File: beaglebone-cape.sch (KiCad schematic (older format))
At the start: 9 parts, among them J1 CONN_2X2, P1 BEAGLEBONE_BLACK, U1 24C16

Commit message: Create the io cape base on the barebone cape
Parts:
- removed J1: CONN_2X2, symbol CONN_2X2
- added C10, C11, C3, C4, C5, C6, C8, C9: C, Capacitors_SMD:C_0805, symbol C
- added C2, C7: CP2, Capacitors_SMD:c_elec_6.3x5.7, symbol CP2
- added CON1: USB-MICRO-B, Connect:USB_Micro-B, symbol USB-MICRO-B
- added J1: CONN_02X02, Pin_Headers:Pin_Header_Straight_2x02, symbol CONN_02X02
- added J5vSelect1: CONN_01X03, Pin_Headers:Pin_Header_Straight_1x03, symbol CONN_01X03
- added J_ADC_REF1, P_PWR1: CONN_01X02, Pin_Headers:Pin_Header_Straight_1x02, symbol CONN_01X02
- added P0+1, P0-1, P0S1, P1+1, P1-1, P1S1, P2+1, P2-1, P2S1, P8, PIO1, PIO_3V3, PIO_5V1, PIO_GND1, P_AD+1, P_AD-1, P_AD1: CONN_01X08, Pin_Headers:Pin_Header_Straight_1x08, symbol CONN_01X08
- added UADC1: ADS7828, Housings_SSOP:TSSOP-16_4.4x5mm_Pitch0.65mm, symbol ADS7828
- added UP0, UP1, UP2, UPIO1: TXS0108E, Housings_SSOP:TSSOP-20_4.4x6.5mm_Pitch0.65mm, symbol TXS0108E
- added U_IMU1: BMX055-Breakout, Pin_Headers:Pin_Header_Straight_1x10, symbol BMX055-Breakout
- C1: footprint ~ -> Capacitors_SMD:C_0805
- P1: footprint ~ -> BeagleBoneBlack Cape:BEAGLEBONE_BLACK
- R1, R2, R3, R4, R5: footprint ~ -> Resistors_SMD:R_0805
- U_EEPROM1: renamed from U1; footprint (none) -> SMD_Packages:SOIC-8-W
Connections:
- net labels added: ECAPPWM0, ECAPPWM2, EHRPWM0A, EHRPWM0B, P_GPIO_32, P_GPIO_33, P_GPIO_34, P_GPIO_35, P_GPIO_36, P_GPIO_37, P_GPIO_38, P_GPIO_39, P_GPIO_70, P_GPIO_71, P_GPIO_72, P_GPIO_73, P_GPIO_74, P_GPIO_75, P_GPIO_76, P_GPIO_77, P_I2C2_SCL, P_I2C2_SDA, P_PWM_P8_13, P_PWM_P8_19, P_PWM_P9_14, P_PWM_P9_16, P_PWM_P9_28, P_PWM_P9_29, P_PWM_P9_31, P_PWM_P9_42, P_SPI0_CS0, P_SPI0_D0, P_SPI0_D1, P_SPI0_SCLK, P_UART1_RXD, P_UART1_TXD, SHLD_5V, SPI0_CS0, SPI0_D0, SPI0_D1, SPI0_SCLK
- wire segments 24 -> 117
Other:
- note removed: "BEAGLEBONE HEADERS"
- moved on the sheet: C1, P1A, P1B, R1, R2, R3, R4, R5, U_EEPROM1

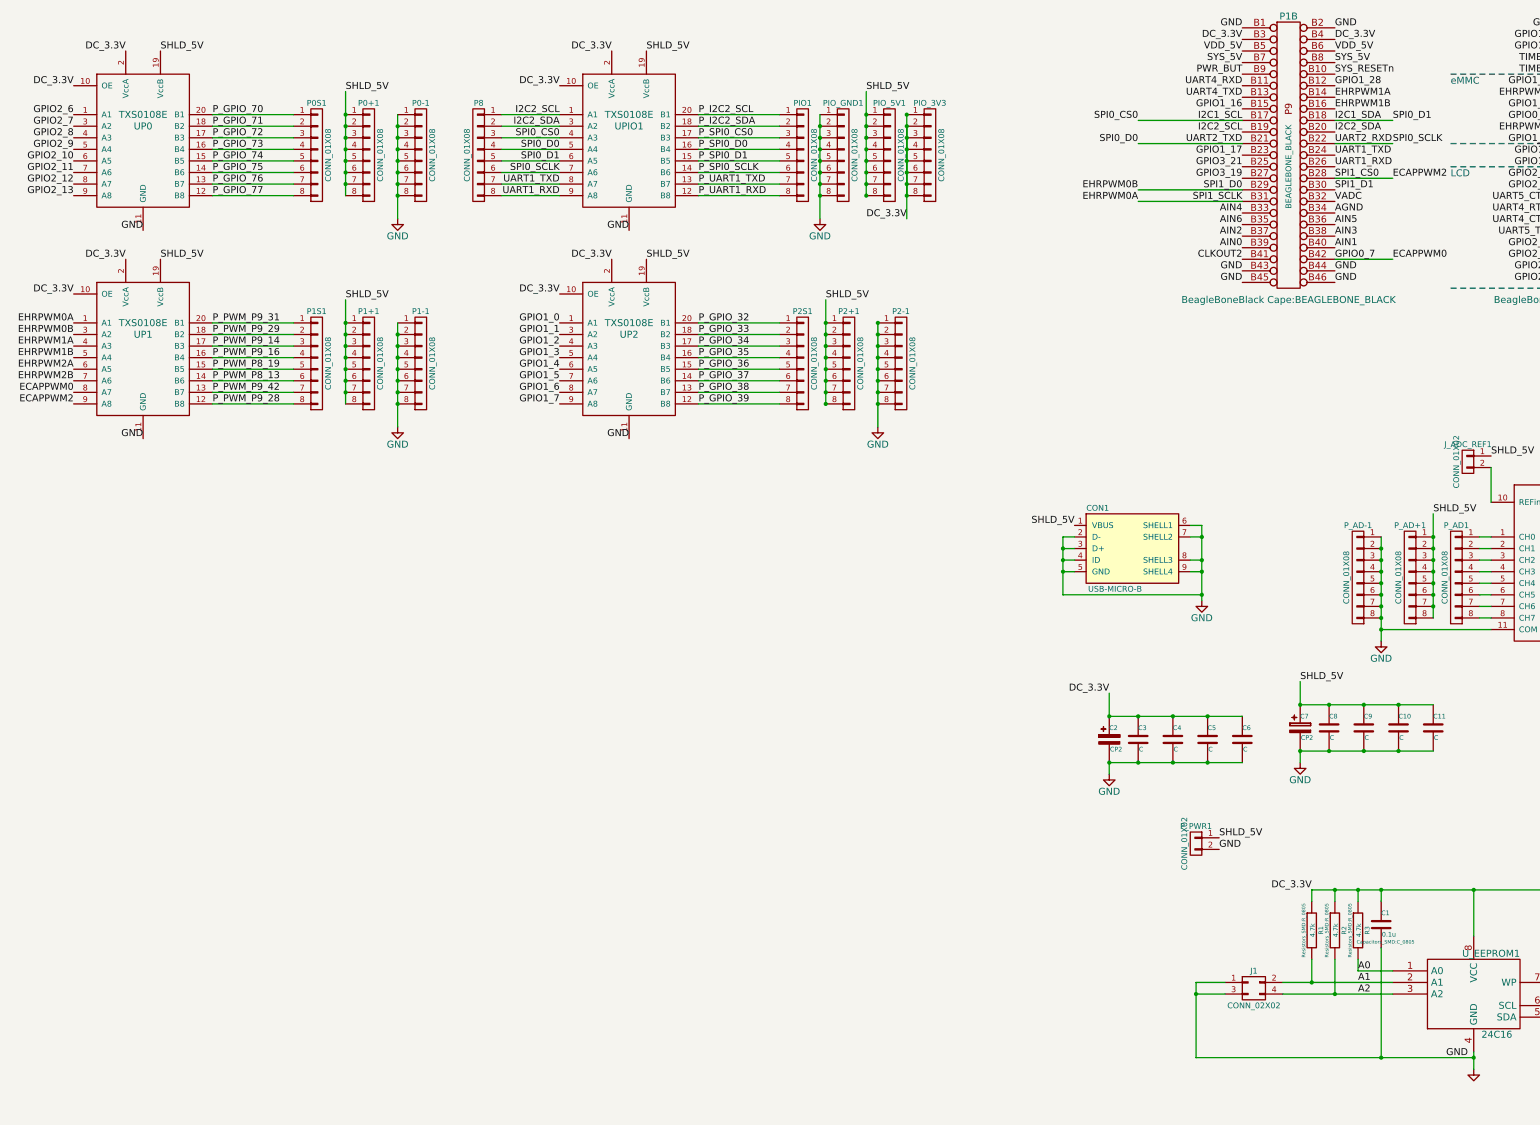
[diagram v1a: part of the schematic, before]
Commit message: Added new symbols for new ICs, created gitignore
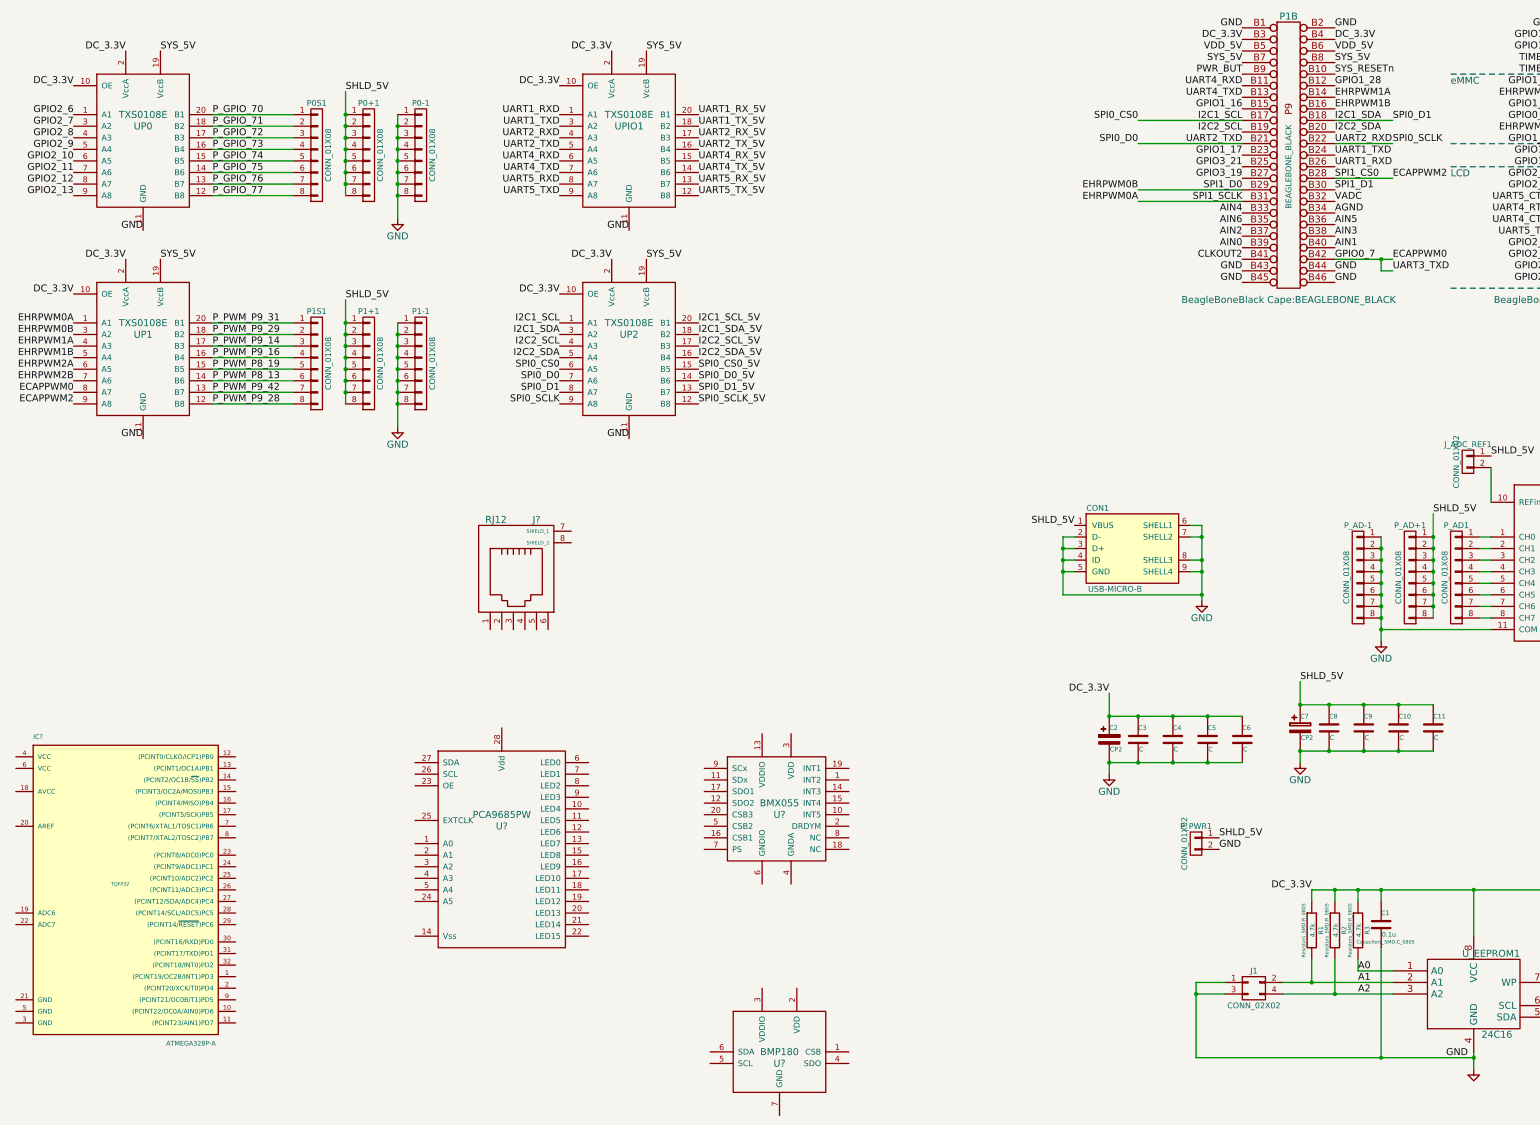
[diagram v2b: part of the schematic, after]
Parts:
- removed P2+1, P2-1, P2S1, P8, PIO1, PIO_3V3, PIO_5V1, PIO_GND1: CONN_01X08, Pin_Headers:Pin_Header_Straight_1x08, symbol CONN_01X08
- added IC?: ATMEGA328P-A, TQFP32, symbol ATMEGA328P-A
- added J?: RJ12, symbol RJ12
- added U?: PCA9685PW, symbol PCA9685PW
- added U?: BMX055, symbol BMX055
- added U?: BMP180, symbol BMP180
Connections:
- net GPIO1_0: no longer UP2.1 (A1)
- net GPIO1_1: no longer UP2.3 (A2)
- net GPIO1_2: no longer UP2.4 (A3)
- net GPIO1_3: no longer UP2.5 (A4)
- net GPIO1_4: no longer UP2.6 (A5)
- net GPIO1_5: no longer UP2.7 (A6)
- net GPIO1_6: no longer UP2.8 (A7)
- net GPIO1_7: no longer UP2.9 (A8)
- net I2C1_SCL: now also UP2.1 (A1), UP2.6 (A5); no longer UPIO1.4 (A3)
- net I2C1_SDA: now also UP2.3 (A2), UP2.8 (A7); no longer UPIO1.6 (A5)
- net I2C2_SCL: now also UP2.4 (A3); no longer UPIO1.1 (A1)
- net I2C2_SDA: now also UP2.5 (A4); no longer UPIO1.3 (A2)
- net P_I2C2_SCL: no longer UPIO1.20 (B1)
- net P_I2C2_SDA: no longer UPIO1.18 (B2)
- net SHLD_5V: no longer UP0.19 (VccB), UP1.19 (VccB), UP2.19 (VccB), UPIO1.19 (VccB)
- net SPI0_D0: now also UP2.7 (A6)
- net SPI0_SCLK: now also UP2.9 (A8), UPIO1.4 (A3); no longer UPIO1.7 (A6)
- net SYS_5V: now also UP0.19 (VccB), UP1.19 (VccB), UP2.19 (VccB), UPIO1.19 (VccB)
- net UART1_RXD: now also UPIO1.1 (A1); no longer UPIO1.9 (A8)
- net UART1_TXD: now also UPIO1.3 (A2); no longer UPIO1.8 (A7)
- net UART4_RXD: now also UPIO1.6 (A5)
- net UART4_TXD: now also UPIO1.7 (A6)
- net UART5_RXD: now also UPIO1.8 (A7)
- net UART5_TXD: now also UPIO1.9 (A8)
- net P_GPIO_32 renamed I2C1_SCL_5V
- net P_GPIO_33 renamed I2C1_SDA_5V
- net P_GPIO_34 renamed I2C2_SCL_5V
- net P_GPIO_35 renamed I2C2_SDA_5V
- net P_GPIO_36 renamed SPI0_CS0_5V
- net P_GPIO_37 renamed SPI0_D0_5V
- net P_GPIO_38 renamed SPI0_D1_5V
- net P_GPIO_39 renamed SPI0_SCLK_5V
- net P_SPI0_CS0 renamed UART2_RX_5V
- net P_SPI0_D0 renamed UART2_TX_5V
- net P_SPI0_D1 renamed UART4_RX_5V
- net P_SPI0_SCLK renamed UART4_TX_5V
- net P_UART1_RXD renamed UART5_TX_5V
- net P_UART1_TXD renamed UART5_RX_5V
- new net UART1_RX_5V: UPIO1.20 (B1)
- new net UART1_TX_5V: UPIO1.18 (B2)

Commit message: Create schematics for plane shield
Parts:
- removed U_IMU1: BMX055-Breakout, Pin_Headers:Pin_Header_Straight_1x10, symbol BMX055-Breakout
- added C? (x3): 0.1uf, symbol C
- added D?: LED, symbol LED
- added J? (x4): RJ12, symbol RJ12
- added JP? (x2): JUMPER, symbol JUMPER
- added P? (x3): CONN_01X14, symbol CONN_01X14
- added P?: CONN_01X02, symbol CONN_01X02
- added P?: CONN_02X08, symbol CONN_02X08
- added P?: CONN_02X03, symbol CONN_02X03
- added P? (x4): CONN_01X06, symbol CONN_01X06
- added P?: CONN_01X04, symbol CONN_01X04
- added PPM_IN1, SERIAL_IN: CONN_01X03, symbol CONN_01X03
- added R?: 330, symbol R
- added R?: 10K, symbol R
- added R?: 10k, symbol R
- added SW?: SW_PUSH, symbol SW_PUSH
- added X?: CRYSTAL_SMD, symbol CRYSTAL_SMD
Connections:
- net A0: now also IC?.23 ((PCINT8/ADC0)PC0), P?.10 (P10)
- net A1: now also IC?.24 ((PCINT9/ADC1)PC1), P?.12 (P12)
- net A2: now also IC?.25 ((PCINT10/ADC2)PC2), P?.14 (P14)
- net DC_3.3V: now also U?.13 (VDDIO), U?.2 (VDD), U?.3 (VDD), U?.3 (VDDIO), U?.7 (PS); no longer UP0.10 (OE), UP1.10 (OE), UP2.10 (OE), UPIO1.10 (OE)
- net GND: now also IC?.21 (GND), IC?.3 (GND), IC?.5 (GND), J?.2, U?.1 (A0), U?.12 (SDO2), U?.14 (Vss), U?.17 (SDO1), U?.2 (A1), U?.20 (CSB3), U?.24 (A5), U?.25 (EXTCLK), U?.3 (A2), U?.4 (A3), U?.4 (GNDA), U?.5 (A4), U?.6 (GNDIO), U?.7 (GND), C?.2, C?.2, D?.2 (K), J?.2, J?.2, J?.2, J?.2, P?.1 (P1), P?.1 (P1), P?.10 (P10), P?.11 (P11), P?.12 (P12), P?.13 (P13), P?.14 (P14), P?.2 (P2), P?.2 (P2), P?.3 (P3), P?.4 (P4), P?.4 (P4), P?.5 (P5), P?.6 (P6), P?.6 (P6), P?.6 (P6), P?.6 (P6), P?.6 (P6), P?.7 (P7), P?.8 (P8), P?.9 (P9), PPM_IN1.3 (P3), SERIAL_IN.2 (P2), SW?.2, X?.3 (case)
- net I2C2_SCL: now also U?.5 (SCL), U?.9 (SCx)
- net I2C2_SCL_5V: now also J?.1, JP?.2, P?.2 (P2)
- net I2C2_SDA: now also U?.11 (SDx), U?.6 (SDA)
- net I2C2_SDA_5V: now also J?.6, JP?.2, P?.3 (P3)
- net SHLD_5V: no longer CON1.1 (VBUS), J5vSelect1.2 (P2), J_ADC_REF1.1 (P1), P0+1.1 (P1), P0+1.2 (P2), P0+1.3 (P3), P0+1.4 (P4), P0+1.5 (P5), P0+1.6 (P6), P0+1.7 (P7), P0+1.8 (P8), P1+1.1 (P1), P1+1.2 (P2), P1+1.3 (P3), P1+1.4 (P4), P1+1.5 (P5), P1+1.6 (P6), P1+1.7 (P7), P1+1.8 (P8), P_AD+1.1 (P1), P_AD+1.2 (P2), P_AD+1.3 (P3), P_AD+1.4 (P4), P_AD+1.5 (P5), P_AD+1.6 (P6), P_AD+1.7 (P7), P_AD+1.8 (P8), UADC1.16 (Vdd)
- net SPI0_CS0_5V: now also J?.1
- net SPI0_D0_5V: now also J?.3
- net SPI0_D1_5V: now also J?.4
- net SPI0_SCLK_5V: now also J?.6
- net SYS_5V: now also J_ADC_REF1.1 (P1), UADC1.16 (Vdd)
- net SYS_RESETn: now also UP0.10 (OE), UP1.10 (OE), UP2.10 (OE), UPIO1.10 (OE)
- net UART1_RX_5V: now also J?.4, P?.3 (P3)
- net UART1_TX_5V: now also J?.3, P?.2 (P2)
- net UART2_RX_5V: now also J?.4, P?.3 (P3)
- net UART2_TX_5V: now also J?.3, P?.2 (P2)
- net UART4_RX_5V: now also J?.4, P?.3 (P3)
- net UART4_TX_5V: now also J?.3, P?.2 (P2)
- net UART5_RX_5V: now also IC?.31 ((PCINT17/TXD)PD1), J?.4, P?.5 (P5)
- net UART5_TX_5V: now also IC?.30 ((PCINT16/RXD)PD0), J?.3, P?.4 (P4), SERIAL_IN.1 (P1)
- net D3: now reaches IC?.1 ((PCINT19/OC2B/INT1)PD3)
- net D3: now also P?.3 (P3)
- net D6: now reaches IC?.10 ((PCINT22/OC0A/AIN0)PD6)
- net D6: now also P?.9 (P9)
- net D7: now reaches IC?.11 ((PCINT23/AIN1)PD7)
- net D7: now also P?.11 (P11)
- net D8: now reaches IC?.12 ((PCINT0/CLKO/ICP1)PB0)
- net D8: now also P?.13 (P13)
- net D9: now reaches IC?.13 ((PCINT1/OC1A)PB1)
- net D9: now also P?.15 (P15)
- net D10: now reaches IC?.14 ((PCINT2/OC1B/~SS~)PB2)
- net D10: now also P?.2 (P2)
- net D11: now reaches IC?.15 ((PCINT3/OC2A/MOSI)PB3)
- net D11: now also P?.4 (P4), P?.4 (P4)
- net D12: now reaches IC?.16 ((PCINT4/MISO)PB4)
- net D12: now also P?.1 (P1), P?.6 (P6)
- net D13: now reaches IC?.17 ((PCINT5/SCK)PB5)
- net D13: now also P?.3 (P3), P?.8 (P8), R?.1
- net PWR_5V: now reaches IC?.18 (AVCC)
- net PWR_5V: now also CON1.1 (VBUS), IC?.4 (VCC), IC?.6 (VCC), J5vSelect1.2 (P2), J?.5, P0+1.1 (P1), P0+1.2 (P2), P0+1.3 (P3), P0+1.4 (P4), P0+1.5 (P5), P0+1.6 (P6), P0+1.7 (P7), P0+1.8 (P8), P1+1.1 (P1), P1+1.2 (P2), P1+1.3 (P3), P1+1.4 (P4), P1+1.5 (P5), P1+1.6 (P6), P1+1.7 (P7), P1+1.8 (P8), P_AD+1.1 (P1), P_AD+1.2 (P2), P_AD+1.3 (P3), P_AD+1.4 (P4), P_AD+1.5 (P5), P_AD+1.6 (P6), P_AD+1.7 (P7), P_AD+1.8 (P8), U?.28 (Vdd), C?.1, J?.5, J?.5, J?.5, J?.5, P?.1 (P1), P?.1 (P1), P?.1 (P1), P?.1 (P1), P?.2 (P2), P?.2 (P2), P?.3 (P3), PPM_IN1.2 (P2), R?.1, R?.1, SERIAL_IN.3 (P3)
- net D4: now reaches IC?.2 ((PCINT20/XCK/T0)PD4)
- net D4: now also P?.5 (P5)
- net at IC?.20 (AREF): now also C?.1
- net A3: now reaches IC?.26 ((PCINT11/ADC3)PC3)
- net A3: now also P?.16 (P16)
- net PWM_SDA: now reaches IC?.27 ((PCINT12/SDA/ADC4)PC4)
- net PWM_SDA: now also U?.27 (SDA), JP?.1
- net PWM_SCL: now reaches IC?.28 ((PCINT14/SCL/ADC5)PC5)
- net PWM_SCL: now also U?.26 (SCL), JP?.1
- net A_RST: now reaches IC?.29 ((PCINT14/~RESET~)PC6)
- net A_RST: now also C?.2, P?.5 (P5), R?.2, SW?.1
- net D2: now reaches IC?.32 ((PCINT18/INT0)PD2)
- net D2: now also P?.1 (P1), PPM_IN1.1 (P1)
- net at IC?.7 ((PCINT6/XTAL1/TOSC1)PB6): now also X?.2
- net at IC?.8 ((PCINT7/XTAL2/TOSC2)PB7): now also X?.1
- net D5: now reaches IC?.9 ((PCINT21/OC0B/T1)PD5)
- net D5: now also P?.7 (P7)
- net at U?.10 (LED4): now also P?.5 (P5)
- net at U?.11 (LED5): now also P?.6 (P6)
- net at U?.12 (LED6): now also P?.7 (P7)
- net at U?.13 (LED7): now also P?.8 (P8)
- net at U?.15 (LED8): now also P?.9 (P9)
- net at U?.16 (LED9): now also P?.10 (P10)
- net at U?.17 (LED10): now also P?.11 (P11)
- net at U?.18 (LED11): now also P?.12 (P12)
- net at U?.19 (LED12): now also P?.13 (P13)
- net at U?.20 (LED13): now also P?.14 (P14)
- net at U?.23 (OE): now also R?.2
- net at U?.6 (LED0): now also P?.1 (P1)
- net at U?.7 (LED1): now also P?.2 (P2)
- net at U?.8 (LED2): now also P?.3 (P3)
- net at U?.9 (LED3): now also P?.4 (P4)
- new net: D?.1 (A), R?.2
- new net DTR: C?.1, J?.6, P?.6 (P6)
- new net SERVO_5V: P?.1 (P1), P?.1 (P1), P?.10 (P10), P?.11 (P11), P?.12 (P12), P?.13 (P13), P?.14 (P14), P?.2 (P2), P?.3 (P3), P?.4 (P4), P?.5 (P5), P?.6 (P6), P?.7 (P7), P?.8 (P8), P?.9 (P9)
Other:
- note added: "1.5 pitch JST-ZH\nFor DSM2 Satellite"
- note added: "Address 0x77"
- note added: "Address: 0x40 (0b1000000)"
- note added: "Address:\n0x18, 0x68, 0x10"
- note added: "Blend i2c on the \nsocket for GPS \nunits which has \nan i2c compass\n"
- note added: "DTR is added\nto pin 6 for \npossible upload\nprogram reset\nusing FTDI\nNOTE: TX RX are \nof BBB, swap for\narduino"
- note added: "FTDI connector"
- note added: "I2C addresses\nBMX055:\n0x18, 0x68, 0x10\n\nBMP180:\n0x77\n\nADS7828:\n0x48\n\n24c16:\n0x50~0x57\n\nPCA9685:\n0x40"
- note added: "ICSP interface"
- moved on the sheet: J?, U?
